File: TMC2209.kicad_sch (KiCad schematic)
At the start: 26 parts, among them J10 Stepper, U7 TMC2209-LA

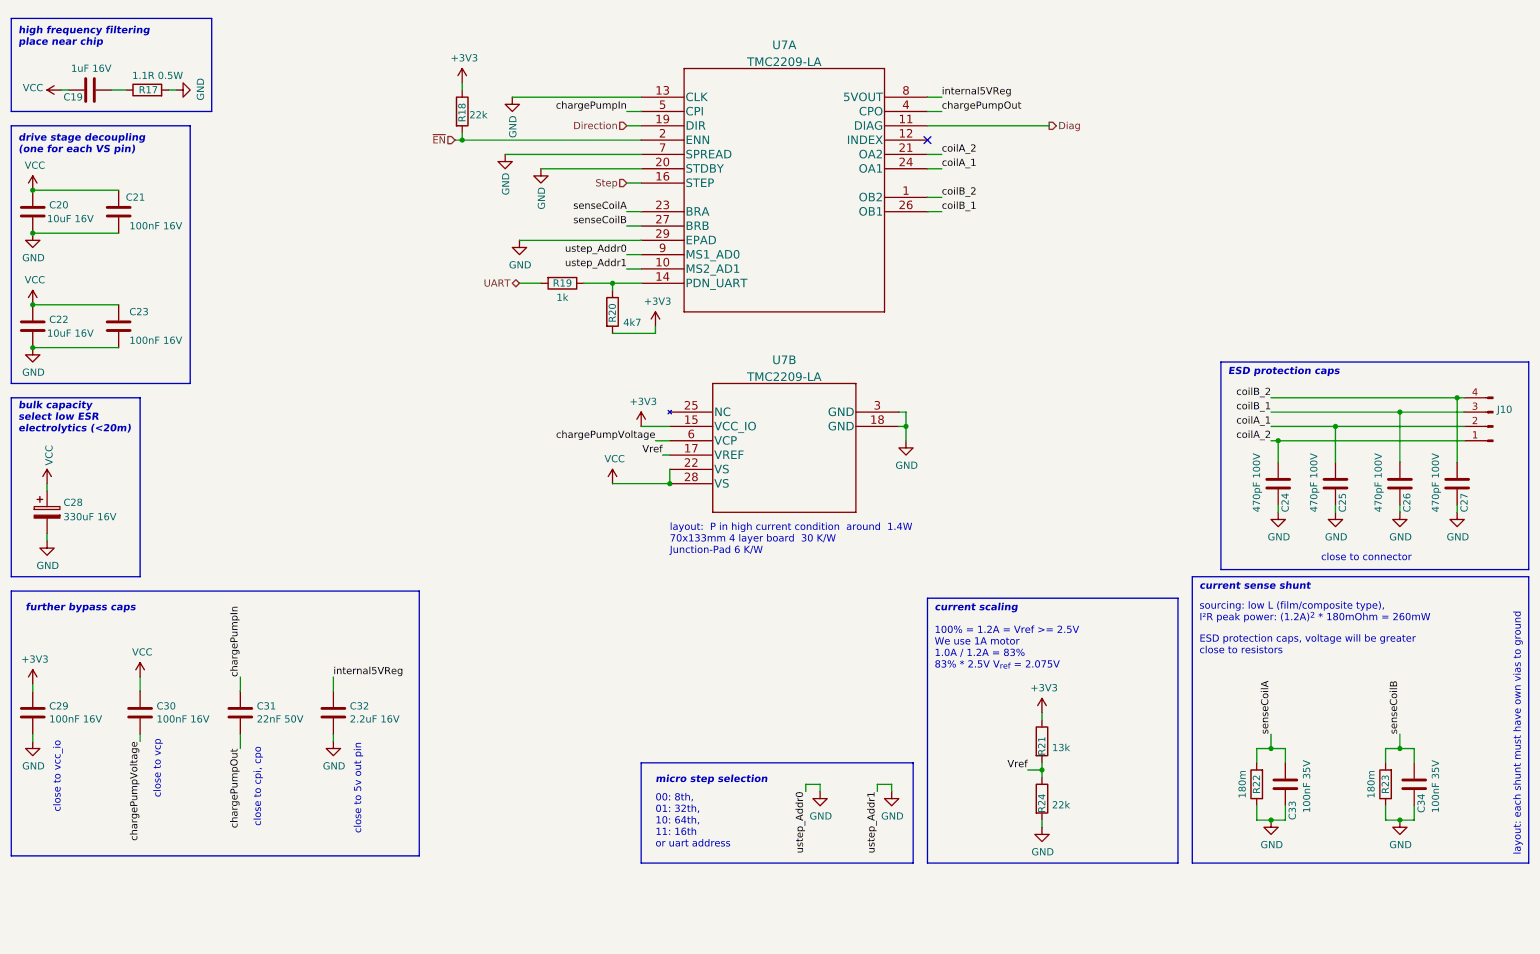
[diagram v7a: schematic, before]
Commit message: Finish PCB layout
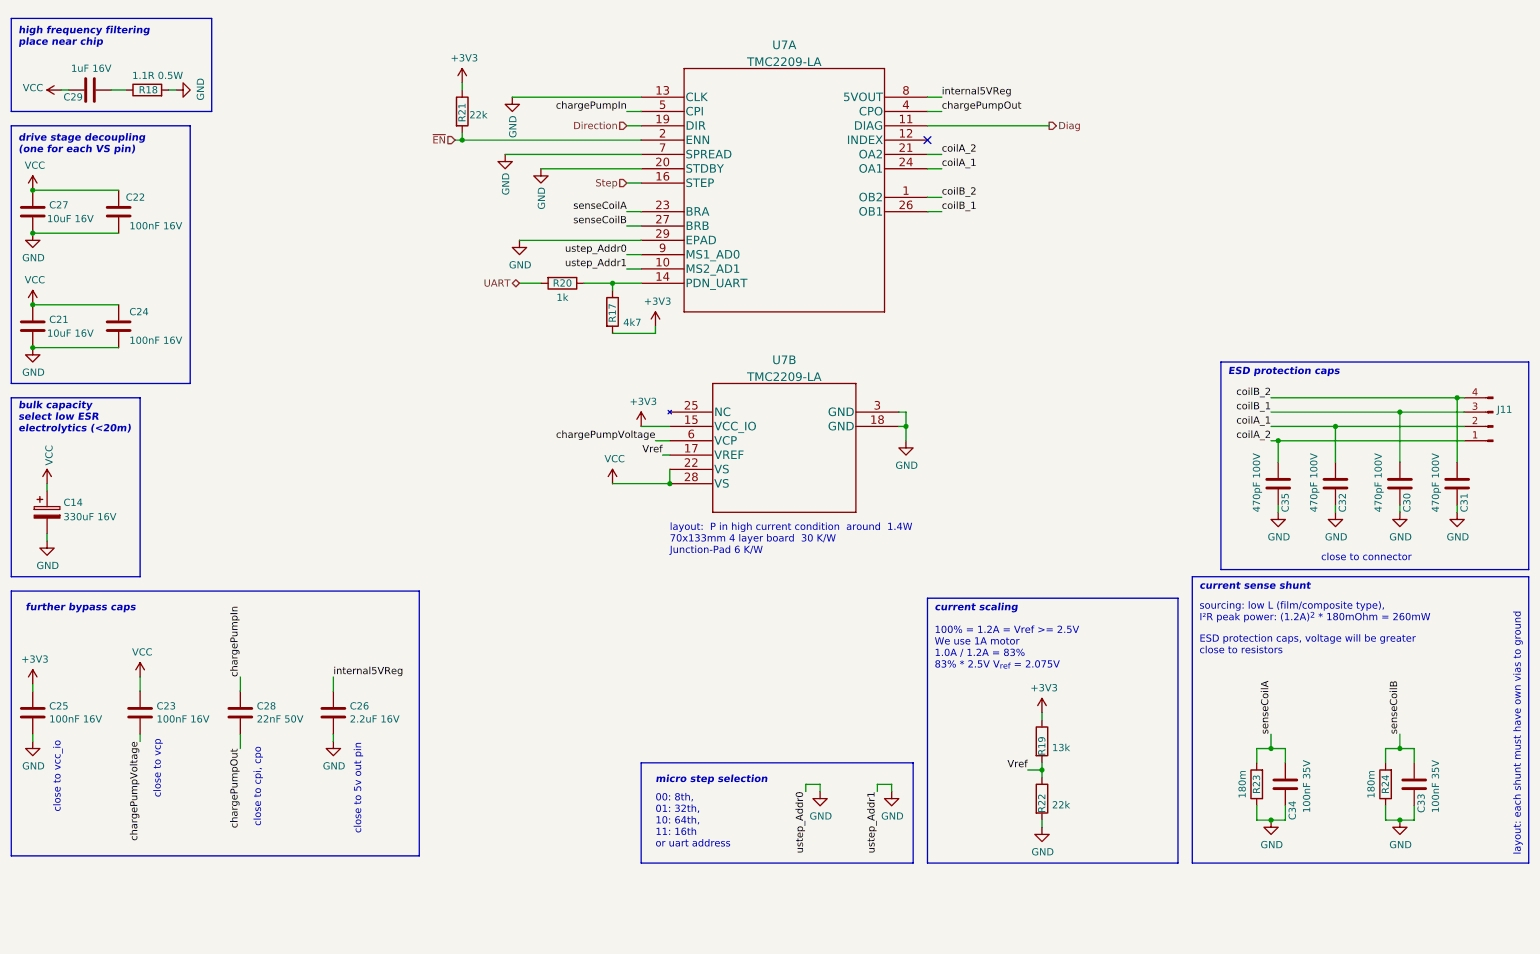
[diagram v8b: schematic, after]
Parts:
- renumbered C28 to C14, C22 to C21, C21 to C22, C30 to C23, C23 to C24, C29 to C25, C32 to C26, C20 to C27, C31 to C28, C19 to C29, C26 to C30, C27 to C31, C25 to C32, C34 to C33, C33 to C34, C24 to C35, J10 to J11, R20 to R17, R17 to R18, R21 to R19, R19 to R20, R18 to R21, R24 to R22, R22 to R23, R23 to R24
